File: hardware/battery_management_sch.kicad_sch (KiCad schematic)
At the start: 29 parts, among them IC1 BQ7791501PWR, IC2 BQ24618RGER, U1 RQ3E100BN, U2 RQ3E100BN

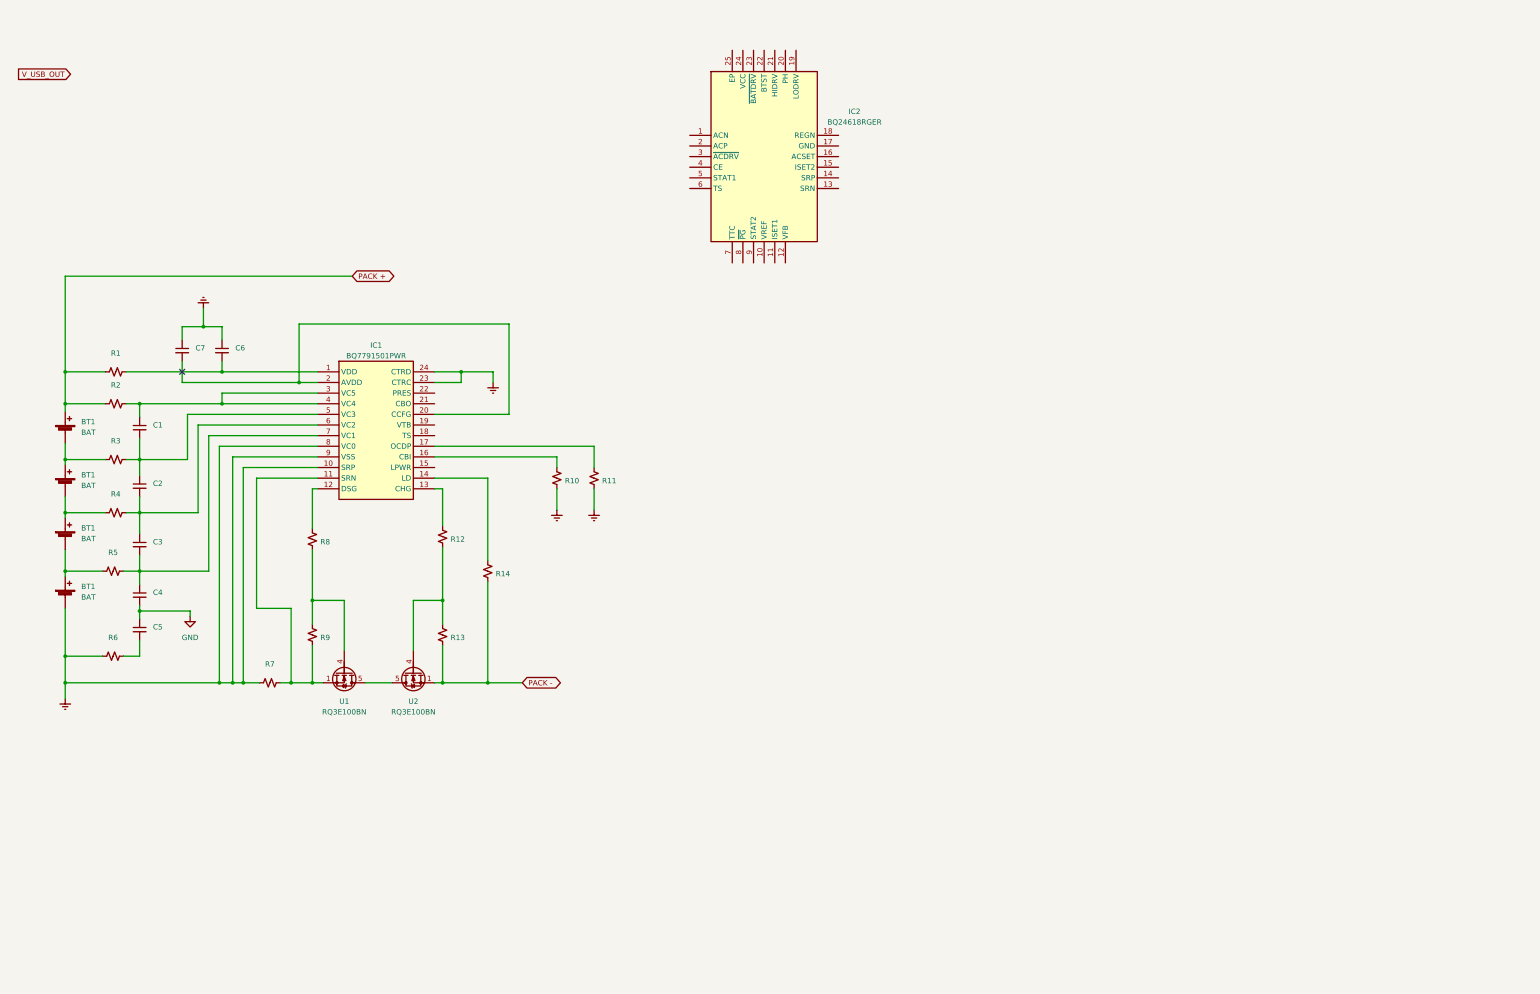
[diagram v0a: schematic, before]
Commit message: Rough schematic of battery charger.
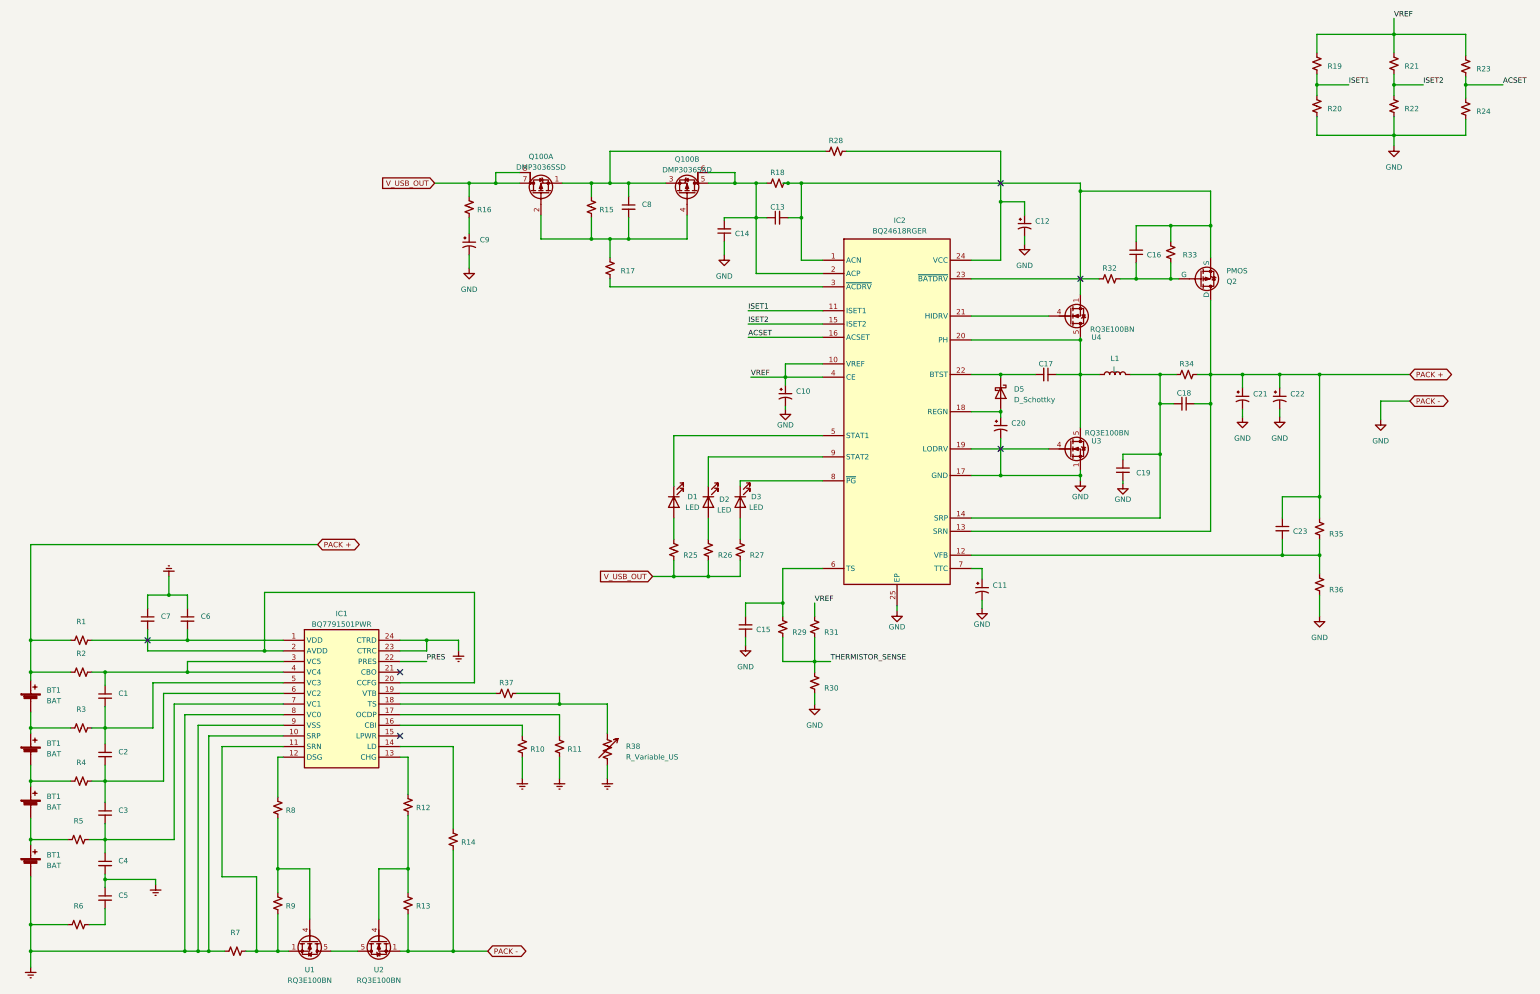
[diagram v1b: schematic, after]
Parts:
- added C10, C11, C12, C20, C21, C22, C9: ~, symbol Device:C_Polarized_Small_US
- added C13, C14, C15, C16, C17, C18, C19, C23, C8: ~, symbol Device:C_Small
- added D1, D2, D3: LED, symbol Device:LED
- added D5: D_Schottky, symbol Device:D_Schottky
- added L1: L, symbol Device:L
- added Q100: DMP3036SSD, Package_SO:SO-8_3.9x4.9mm_P1.27mm, symbol Device:Q_Dual_PMOS_S1G1S2G2D2D2D1D1
- added Q2: PMOS, symbol Simulation_SPICE:PMOS
- added R15, R16, R17, R18, R19, R20, R21, R22, R23, R24, R25, R26, R27, R28, R29, R30, R31, R32, R33, R34, R35, R36, R37: ~, symbol Device:R_Small_US
- added R38: R_Variable_US, symbol Device:R_Variable_US
- added U3, U4: RQ3E100BN, User_Mosfet:HSMT8, symbol User_MOSFET:RQ3E100BN
- IC1: footprint SOP65P640X120-24N -> User_SOP:SOP65P640X120-24N
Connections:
- net PACK - is gone; now on net GND: R13.1, R14.1, U2.1, U2.2, U2.3
- net Earth: now also C4.2, C5.1, R38.2
- net GND: now also IC2.17 (GND), IC2.25 (EP), C10.2, C11.2, C12.2, C14.1, C15.1, C19.2, C20.2, C21.2, C22.2, C9.2, R20.2, R22.2, R24.2, R30.1, R36.1, U3.1, U3.2, U3.3; no longer C4.2, C5.1
- net PACK +: now also IC2.13 (SRN), C18.1, C21.1, C22.1, C23.1, Q2.1 (D), R34.2, R35.2
- net V_USB_OUT: now also Q100.7 (D), Q100.8 (G), R16.2, R25.1, R26.1, R27.1
- net at IC1.18 (TS): now also R37.2, R38.1
- net at IC1.19 (VTB): now also R37.1
- net PRES: now reaches IC1.22 (PRES)
- net at IC2.1 (ACN): now also C13.2, C16.2, Q2.3 (S), R18.2, R33.2, U4.1, U4.2, U4.3
- net VREF: now reaches IC2.10 (VREF)
- net VREF: now also IC2.4 (CE), C10.1, R19.1, R21.1, R23.1, R31.2
- net ISET1: now reaches IC2.11 (ISET1)
- net ISET1: now also R19.2, R20.1
- net at IC2.12 (VFB): now also C23.2, R35.1, R36.2
- net at IC2.14 (SRP): now also C18.2, C19.1, L1.2, R34.1
- net ISET2: now reaches IC2.15 (ISET2)
- net ISET2: now also R21.2, R22.1
- net ACSET: now reaches IC2.16 (ACSET)
- net ACSET: now also R23.2, R24.1
- net at IC2.18 (REGN): now also C20.1, D5.2 (A)
- net at IC2.19 (LODRV): now also U3.4
- net at IC2.2 (ACP): now also C13.1, C14.2, Q100.5 (D), Q100.6 (G), R18.1
- net at IC2.20 (PH): now also C17.1, L1.1, U3.5, U4.5
- net at IC2.21 (HIDRV): now also U4.4
- net at IC2.22 (BTST): now also C17.2, D5.1 (K)
- net at IC2.23 (~{BATDRV}): now also R32.1
- net at IC2.24 (VCC): now also C12.1, R28.2
- net at IC2.3 (~{ACDRV}): now also R17.2
- net at IC2.5 (STAT1): now also D1.1 (K)
- net at IC2.6 (TS): now also C15.2, R29.2
- net at IC2.7 (TTC): now also C11.1
- net at IC2.8 (~{PG}): now also D3.1 (K)
- net at IC2.9 (STAT2): now also D2.1 (K)
- new net: C16.1, Q2.2 (G), R32.2, R33.1
- new net: C8.1, Q100.1 (S), Q100.3 (S), R15.2, R28.1
- new net: C8.2, Q100.2 (G), Q100.4 (G), R15.1, R17.1
- new net: D2.2 (A), R26.2
- new net: D3.2 (A), R27.2
- new net: D1.2 (A), R25.2
- new net: C9.1, R16.1
- new net THERMISTOR_SENSE: R29.1, R30.2, R31.1
- no-connect marks 1 -> 6
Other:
- moved on the sheet: BT1, C1, C2, C3, C4, C5, C6, C7, IC1, IC2, R1, R10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

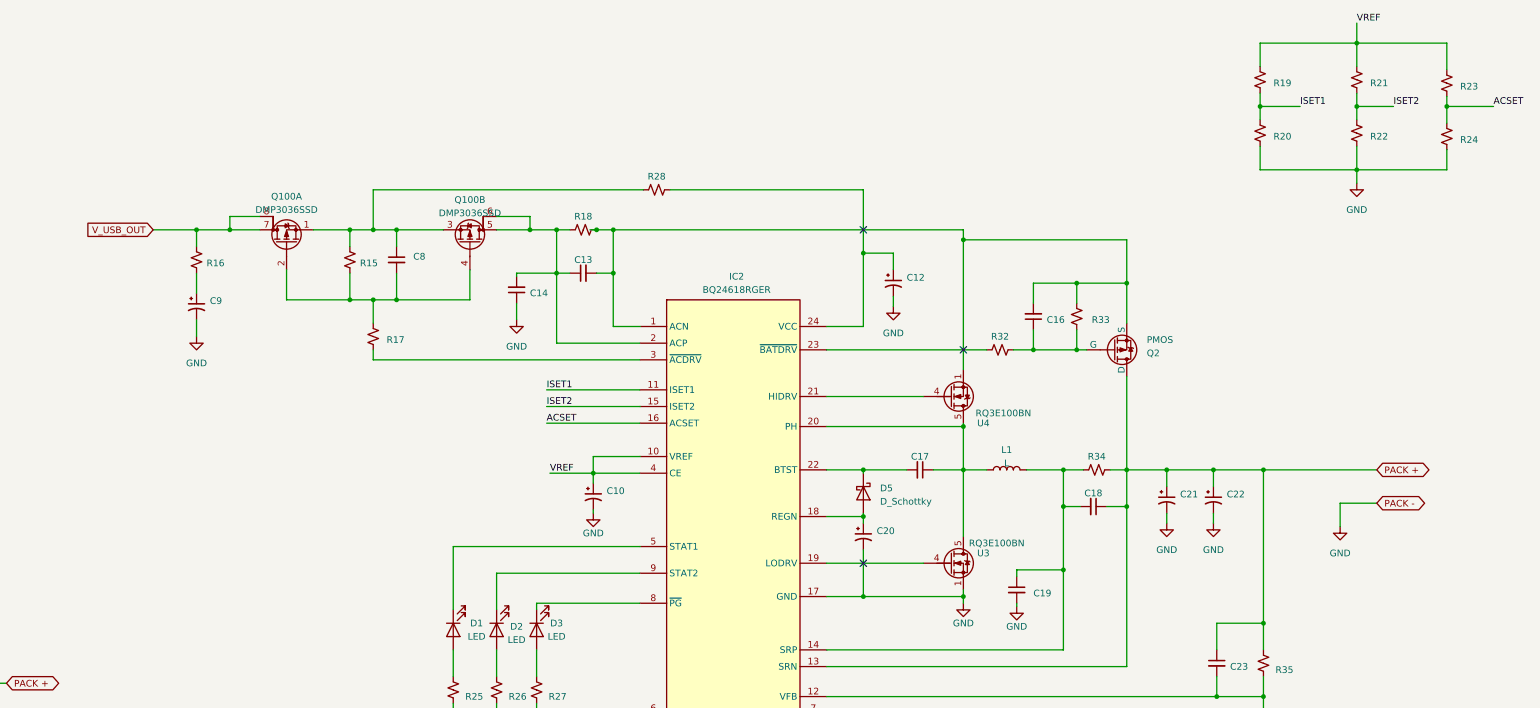
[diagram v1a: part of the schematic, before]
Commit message: Rought draft of battery charger and started SEPIC stage
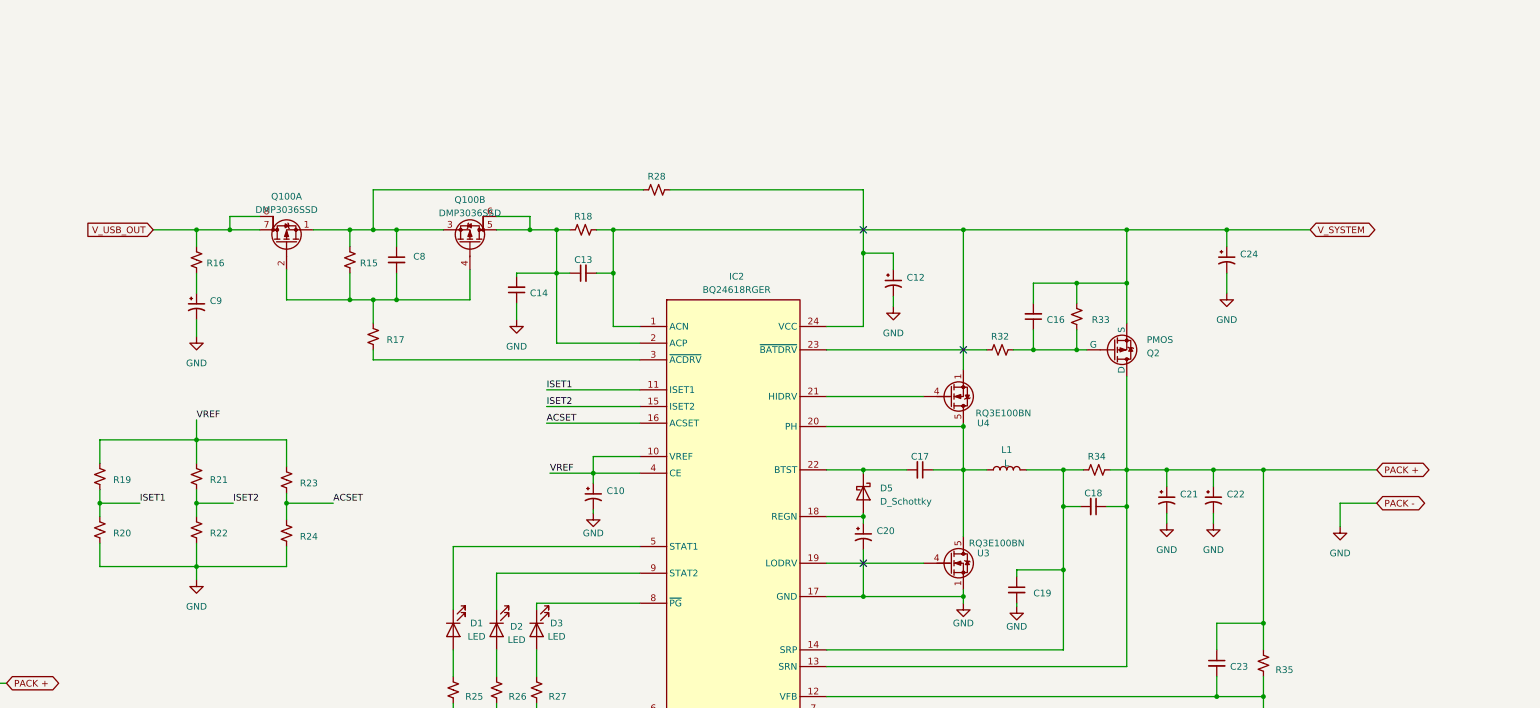
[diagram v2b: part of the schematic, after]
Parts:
- added C24: ~, symbol Device:C_Polarized_Small_US
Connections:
- net GND: now also C24.2
- net V_SYSTEM: now reaches C13.2, C16.2, IC2.1 (ACN), Q2.3 (S), R18.2, R33.2, U4.1, U4.2, U4.3
- net V_SYSTEM: now also C24.1
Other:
- moved on the sheet: R19, R20, R21, R22, R23, R24
